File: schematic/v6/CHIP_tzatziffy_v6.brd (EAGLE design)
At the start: 40.9 x 49.8 mm, 43 parts, among them J1 2X20-CHIP0.8_DRILL, J3 S2B-PH-SM4-TB, Q1 NPN-DTC114YUA, Q2 PNP-DTA114YUA, U1 LMR62421, U3 DS2431P, X1 FH12-40S-0.5SH

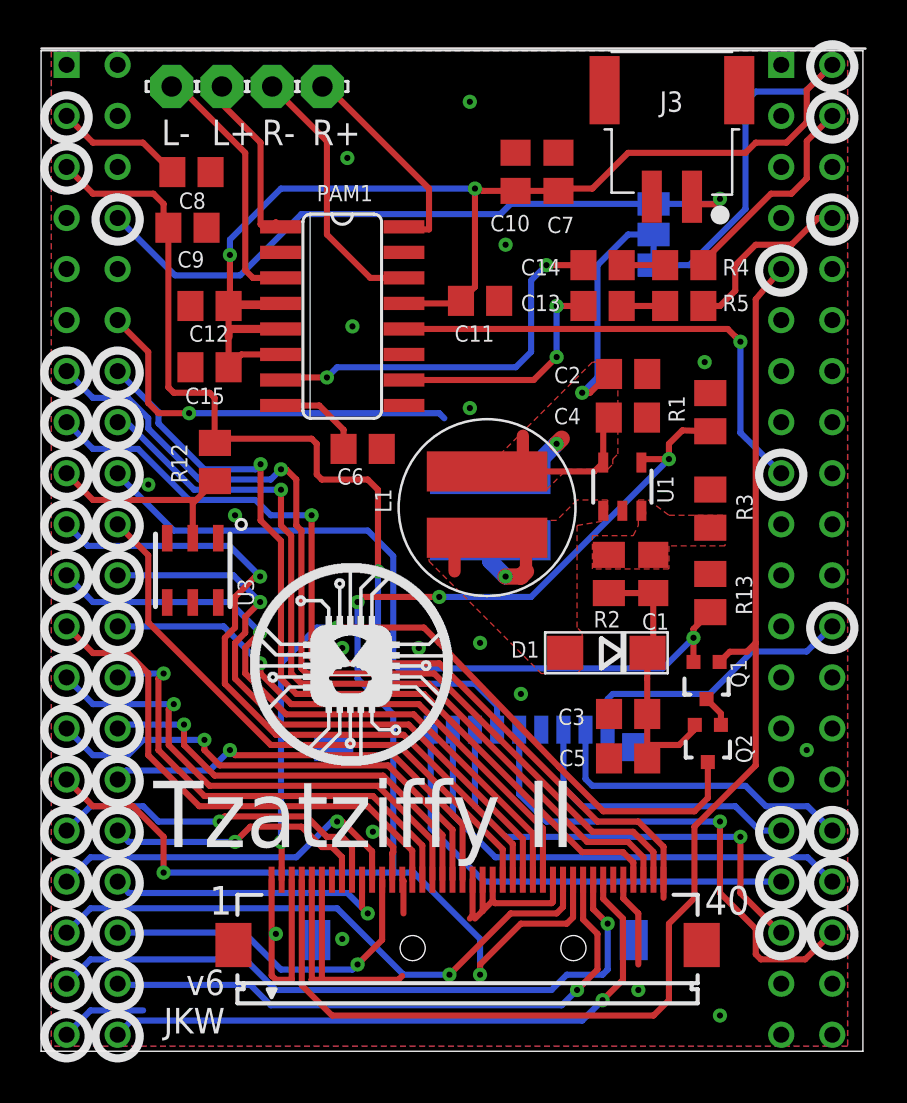
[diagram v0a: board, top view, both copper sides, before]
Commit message: added diode on bottom
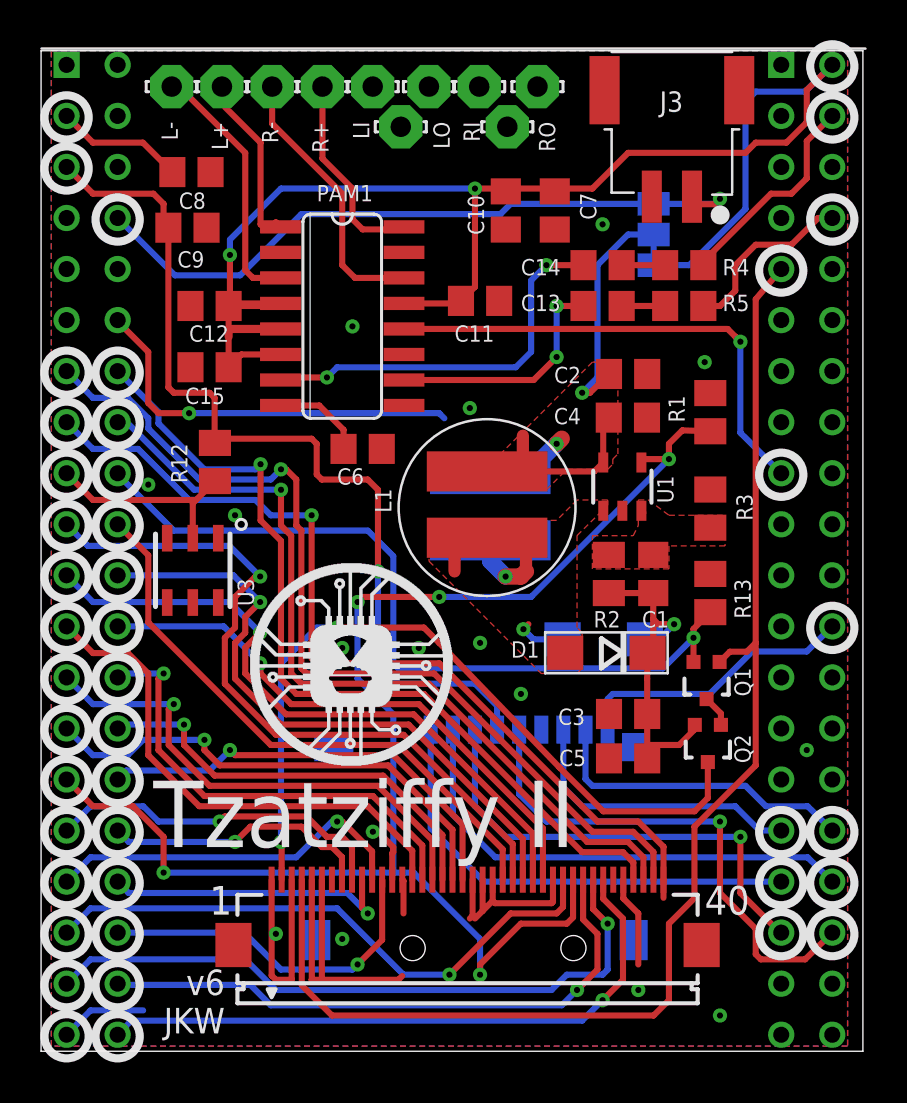
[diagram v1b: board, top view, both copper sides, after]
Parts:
- added D2: B240A, Keyboard v0_5:DO-214AC
- added LG, LI, LO, RG, RI, RO: LSP10, solpad:LSP10
- C8, C9: value 100nF -> n.a.
- moved U$5 9.92 mm to (6.35, 22.4), turned to 90 degrees
- moved U$4 5.31 mm to (6.79, 37.0), turned to 90 degrees
- moved C10 1.98 mm to (23.1, 41.8), turned to 270 degrees
- moved C7 1.93 mm to (25.6, 41.8), turned to 270 degrees
- moved U$3 1.80 mm to (17.5, 36.8), turned to 90 degrees
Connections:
- net GND: now also LG.MP, RG.MP
- net PWR_LGT: now also D2.C
- net VREG_OUTPUT: now also D2.A
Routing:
- net PWR_LGT: track 15.3 -> 18.2 mm, vias 0 -> 1
- net VREG_OUTPUT: track 9.97 -> 12.5 mm, vias 1 -> 2
- net GND: vias 19 -> 17
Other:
- board text added: "CHIPDIPSHOP"
- board text added: "Li"
- board text added: "Lo"
- board text added: "Ri"
- board text added: "Ro"
